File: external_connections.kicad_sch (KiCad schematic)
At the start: 14 parts, among them J1 FTDI_6P, J2 EXT_CLK_IN5, J3 PWR Test, J6 AVR-ISP-6, SW1 SW_Push

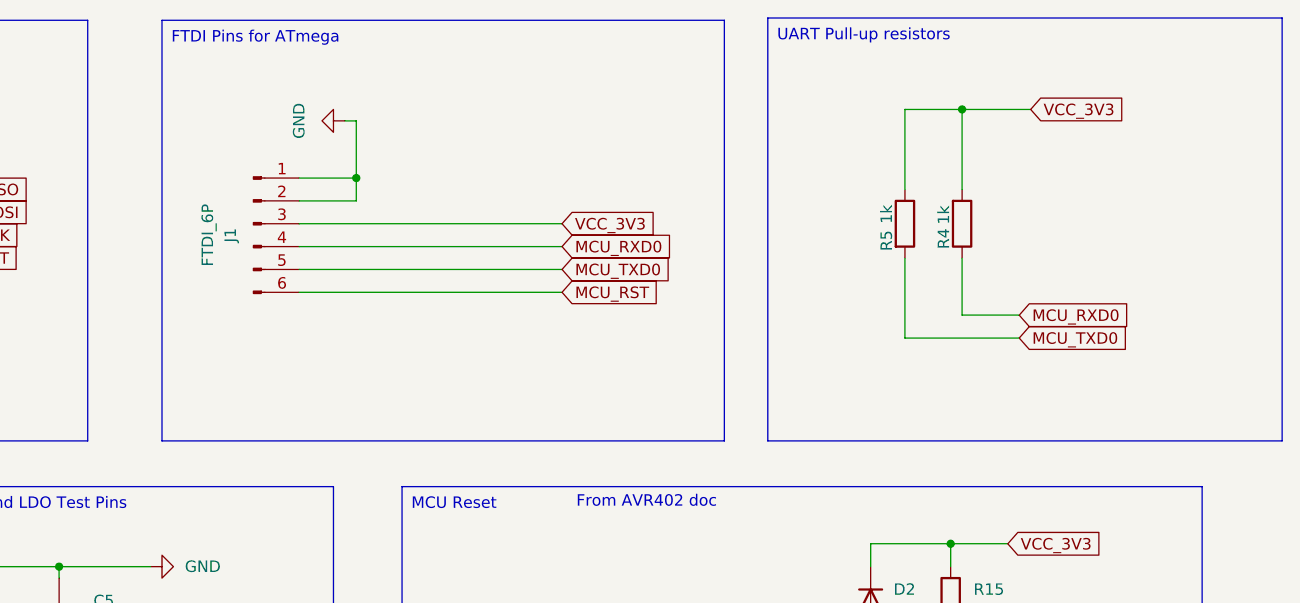
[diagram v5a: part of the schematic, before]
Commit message: inceased the size of some tp headers to 2.00mm
Signed-off-by: Mika Laitio <lamikr@gmail.com>
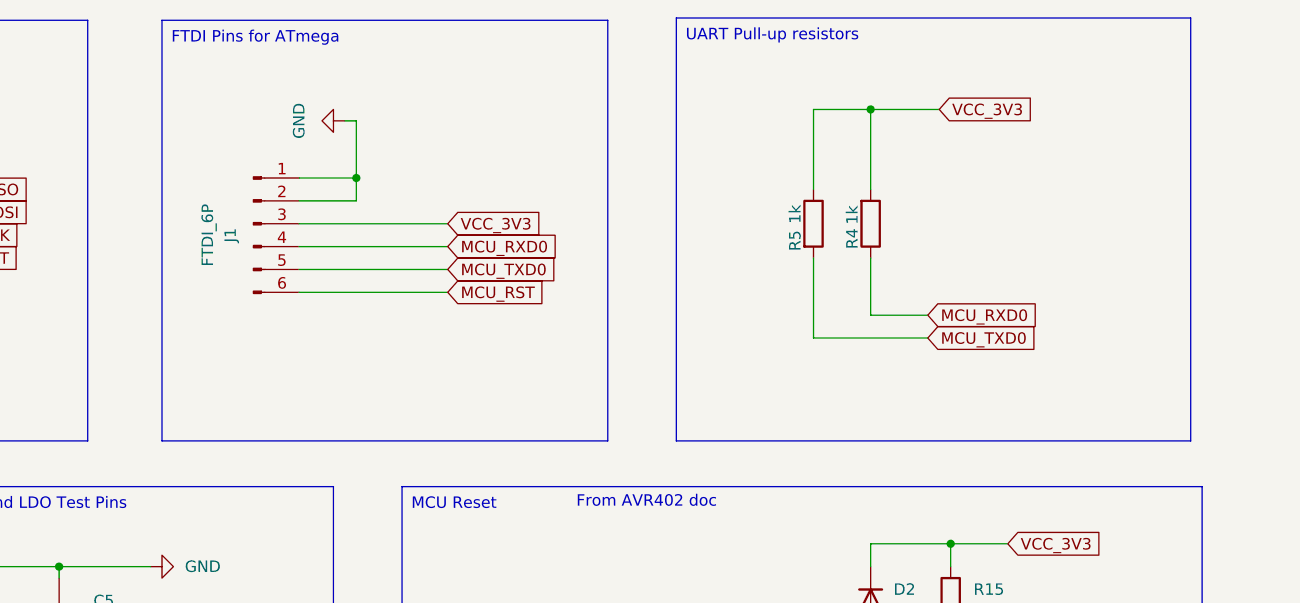
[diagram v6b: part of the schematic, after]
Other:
- moved on the sheet: R4, R5
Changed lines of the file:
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@@
 	)
 	(junction
-		(at 200.66 27.94)
+		(at 190.5 27.94)
 		(diameter 0)
 		(color 0 0 0 0)
@@
 	(wire
 		(pts
-			(xy 200.66 36.83) (xy 200.66 27.94)
-		)
-		(stroke
-			(width 0)
-			(type default)
-		)
-	)
-	(wire
-		(pts
-			(xy 200.66 27.94) (xy 208.28 27.94)
+			(xy 190.5 36.83) (xy 190.5 27.94)
+		)
+		(stroke
+			(width 0)
+			(type default)
+		)
+	)
+	(wire
+		(pts
+			(xy 190.5 27.94) (xy 198.12 27.94)
 		)
 		(stroke
@@
 	(wire
 		(pts
-			(xy 127 40.64) (xy 156.21 40.64)
+			(xy 127 40.64) (xy 143.51 40.64)
 		)
 		(stroke
@@
 	(wire
 		(pts
-			(xy 207.01 50.8) (xy 200.66 50.8)
+			(xy 196.85 50.8) (xy 190.5 50.8)
 		)
 		(stroke
@@
 	(wire
 		(pts
-			(xy 207.01 53.34) (xy 194.31 53.34)
+			(xy 196.85 53.34) (xy 184.15 53.34)
 		)
 		(stroke
@@
 	(wire
 		(pts
-			(xy 200.66 50.8) (xy 200.66 44.45)
-		)
-		(stroke
-			(width 0)
-			(type default)
-		)
-	)
-	(wire
-		(pts
-			(xy 127 48.26) (xy 156.21 48.26)
+			(xy 190.5 50.8) (xy 190.5 44.45)
+		)
+		(stroke
+			(width 0)
+			(type default)
+		)
+	)
+	(wire
+		(pts
+			(xy 127 48.26) (xy 143.51 48.26)
 		)
 		(stroke
@@
 	(wire
 		(pts
-			(xy 194.31 27.94) (xy 200.66 27.94)
+			(xy 184.15 27.94) (xy 190.5 27.94)
 		)
 		(stroke
@@
 	(wire
 		(pts
-			(xy 194.31 36.83) (xy 194.31 27.94)
+			(xy 184.15 36.83) (xy 184.15 27.94)
 		)
 		(stroke
@@
 	(wire
 		(pts
-			(xy 127 45.72) (xy 156.21 45.72)
+			(xy 127 45.72) (xy 143.51 45.72)
 		)
 		(stroke
@@
 	(wire
 		(pts
-			(xy 194.31 53.34) (xy 194.31 44.45)
+			(xy 184.15 53.34) (xy 184.15 44.45)
 		)
 		(stroke
@@
 	(wire
 		(pts
-			(xy 127 43.18) (xy 156.21 43.18)
+			(xy 127 43.18) (xy 143.51 43.18)
 		)
 		(stroke
@@
 	(text_box "UART Pull-up resistors"
 		(exclude_from_sim no)
-		(at 179.07 17.78 0)
+		(at 168.91 17.78 0)
 		(size 57.15 46.99)
 		(stroke
@@
 		(exclude_from_sim no)
 		(at 111.76 18.034 0)
-		(size 62.484 46.736)
+		(size 49.53 46.736)
 		(stroke
 			(width 0)
@@
 	(global_label "VCC_3V3"
 		(shape input)
-		(at 208.28 27.94 0)
+		(at 198.12 27.94 0)
 		(fields_autoplaced yes)
 		(effects
@@
 		)
 		(property "Intersheetrefs" "${INTERSHEET_REFS}"
-			(at 219.369 27.94 0)
+			(at 209.209 27.94 0)
 			(effects
 				(font
@@
 	(global_label "MCU_RXD0"
 		(shape input)
-		(at 207.01 50.8 0)
+		(at 196.85 50.8 0)
 		(fields_autoplaced yes)
 		(effects
@@
 		)
 		(property "Intersheetrefs" "${INTERSHEET_REFS}"
-			(at 219.9737 50.8 0)
+			(at 209.8137 50.8 0)
 			(effects
 				(font
@@
 	(global_label "MCU_RXD0"
 		(shape input)
-		(at 156.21 43.18 0)
+		(at 143.51 43.18 0)
 		(fields_autoplaced yes)
 		(effects
@@
 		)
 		(property "Intersheetrefs" "${INTERSHEET_REFS}"
-			(at 169.1737 43.18 0)
+			(at 156.4737 43.18 0)
 			(effects
 				(font
@@
 	(global_label "MCU_TXD0"
 		(shape input)
-		(at 207.01 53.34 0)
+		(at 196.85 53.34 0)
 		(fields_autoplaced yes)
 		(effects
@@
 		)
 		(property "Intersheetrefs" "${INTERSHEET_REFS}"
-			(at 219.6713 53.34 0)
+			(at 209.5113 53.34 0)
 			(effects
 				(font
@@
 	(global_label "MCU_TXD0"
 		(shape input)
-		(at 156.21 45.72 0)
+		(at 143.51 45.72 0)
 		(fields_autoplaced yes)
 		(effects
@@
 		)
 		(property "Intersheetrefs" "${INTERSHEET_REFS}"
-			(at 168.8713 45.72 0)
+			(at 156.1713 45.72 0)
 			(effects
 				(font
@@
 	(global_label "VCC_3V3"
 		(shape input)
-		(at 156.21 40.64 0)
+		(at 143.51 40.64 0)
 		(fields_autoplaced yes)
 		(effects
@@
 		)
 		(property "Intersheetrefs" "${INTERSHEET_REFS}"
-			(at 167.299 40.64 0)
+			(at 154.599 40.64 0)
 			(effects
 				(font
@@
 	(global_label "MCU_RST"
 		(shape input)
-		(at 156.21 48.26 0)
+		(at 143.51 48.26 0)
 		(fields_autoplaced yes)
 		(effects
@@
 		)
 		(property "Intersheetrefs" "${INTERSHEET_REFS}"
-			(at 167.6618 48.26 0)
+			(at 154.9618 48.26 0)
 			(effects
 				(font
@@
 	(symbol
 		(lib_id "Device:R")
-		(at 194.31 40.64 0)
+		(at 184.15 40.64 0)
 		(unit 1)
 		(exclude_from_sim no)
@@
 		(dnp no)
 		(property "Reference" "R5"
-			(at 192.278 43.688 90)
+			(at 182.118 43.688 90)
 			(effects
 				(font
@@
 		)
 		(property "Value" "1k"
-			(at 192.278 40.64 90)
+			(at 182.118 40.64 90)
 			(effects
 				(font
@@
 		)
 		(property "Footprint" "Resistor_SMD:R_0402_1005Metric"
-			(at 192.532 40.64 90)
+			(at 182.372 40.64 90)
 			(effects
 				(font
@@
 		)
 		(property "Datasheet" "~"
-			(at 194.31 40.64 0)
+			(at 184.15 40.64 0)
 			(effects
 				(font
@@
 		)
 		(property "Description" "Resistor"
-			(at 194.31 40.64 0)
+			(at 184.15 40.64 0)
 			(effects
 				(font
@@
 		)
 		(property "Notes" ""
-			(at 194.31 40.64 0)
+			(at 184.15 40.64 0)
 			(effects
 				(font
@@
 		)
 		(property "Price" "0.1"
-			(at 194.31 40.64 0)
+			(at 184.15 40.64 0)
 			(effects
 				(font
@@
 		)
 		(property "MFR" "Yageo"
-			(at 194.31 40.64 0)
+			(at 184.15 40.64 0)
 			(effects
 				(font
@@
 		)
 		(property "MPN" "RC0402FR-070RL"
-			(at 194.31 40.64 0)
+			(at 184.15 40.64 0)
 			(effects
 				(font
@@
 		)
 		(property "SKU_DIGIKEY" "311-0.0LRCT-ND"
-			(at 194.31 40.64 0)
+			(at 184.15 40.64 0)
 			(effects
 				(font
@@
 		)
 		(property "QtyOrdered" "100"
-			(at 194.31 40.64 0)
+			(at 184.15 40.64 0)
 			(effects
 				(font
@@
 	(symbol
 		(lib_id "Device:R")
-		(at 200.66 40.64 0)
+		(at 190.5 40.64 0)
 		(mirror x)
 		(unit 1)
@@
 		(dnp no)
 		(property "Reference" "R4"
-			(at 198.628 41.148 90)
+			(at 188.468 41.148 90)
 			(effects
 				(font
@@
 		)
 		(property "Value" "1k"
-			(at 198.628 38.608 90)
+			(at 188.468 38.608 90)
 			(effects
 				(font
@@
 		)
 		(property "Footprint" "Resistor_SMD:R_0402_1005Metric"
-			(at 198.882 40.64 90)
+			(at 188.722 40.64 90)
 			(effects
 				(font
@@
 		)
 		(property "Datasheet" "~"
-			(at 200.66 40.64 0)
+			(at 190.5 40.64 0)
 			(effects
 				(font
@@
 		)
 		(property "Description" "Resistor"
-			(at 200.66 40.64 0)
+			(at 190.5 40.64 0)
 			(effects
 				(font
@@
 		)
 		(property "Notes" ""
-			(at 200.66 40.64 0)
+			(at 190.5 40.64 0)
 			(effects
 				(font
@@
 		)
 		(property "Price" "0.1"
-			(at 200.66 40.64 0)
+			(at 190.5 40.64 0)
 			(effects
 				(font
@@
 		)
 		(property "MFR" "Yageo"
-			(at 200.66 40.64 0)
+			(at 190.5 40.64 0)
 			(effects
 				(font
@@
 		)
 		(property "MPN" "RC0402FR-0710KL"
-			(at 200.66 40.64 0)
+			(at 190.5 40.64 0)
 			(effects
 				(font
@@
 		)
 		(property "SKU_DIGIKEY" "311-10.0KLRCT-ND"
-			(at 200.66 40.64 0)
+			(at 190.5 40.64 0)
 			(effects
 				(font
@@
 		)
 		(property "QtyOrdered" "100"
-			(at 200.66 40.64 0)
-			(effects
-				(font
+			(at 190.5 40.64 0)
+			(effects
+				(font

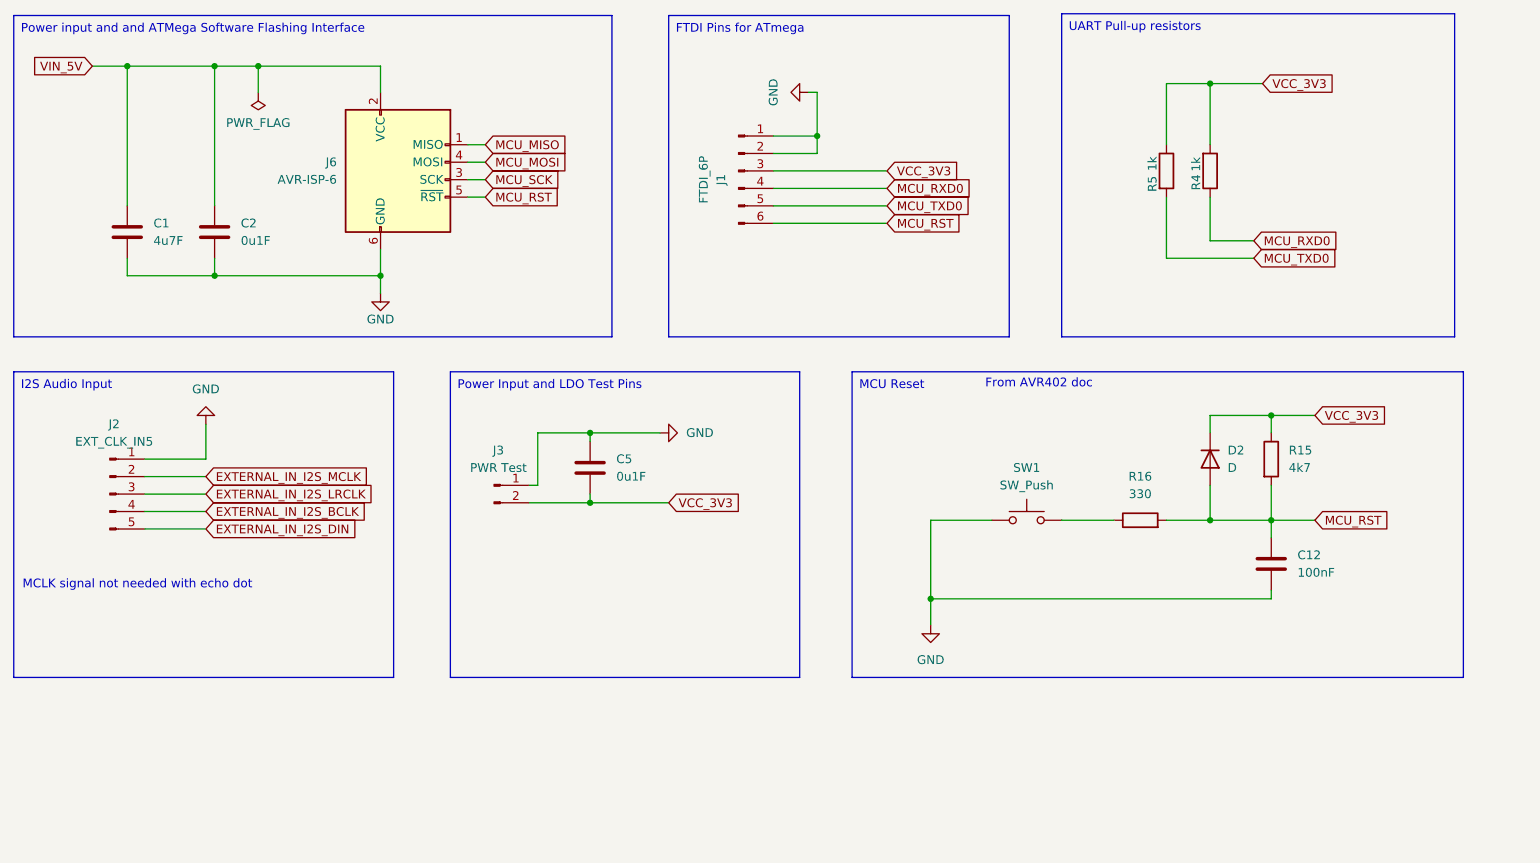
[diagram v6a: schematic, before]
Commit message: component footprint updates
- 0402 caps and resistors to 0603
- reset pin-header to reset button

Signed-off-by: Mika Laitio <lamikr@gmail.com>
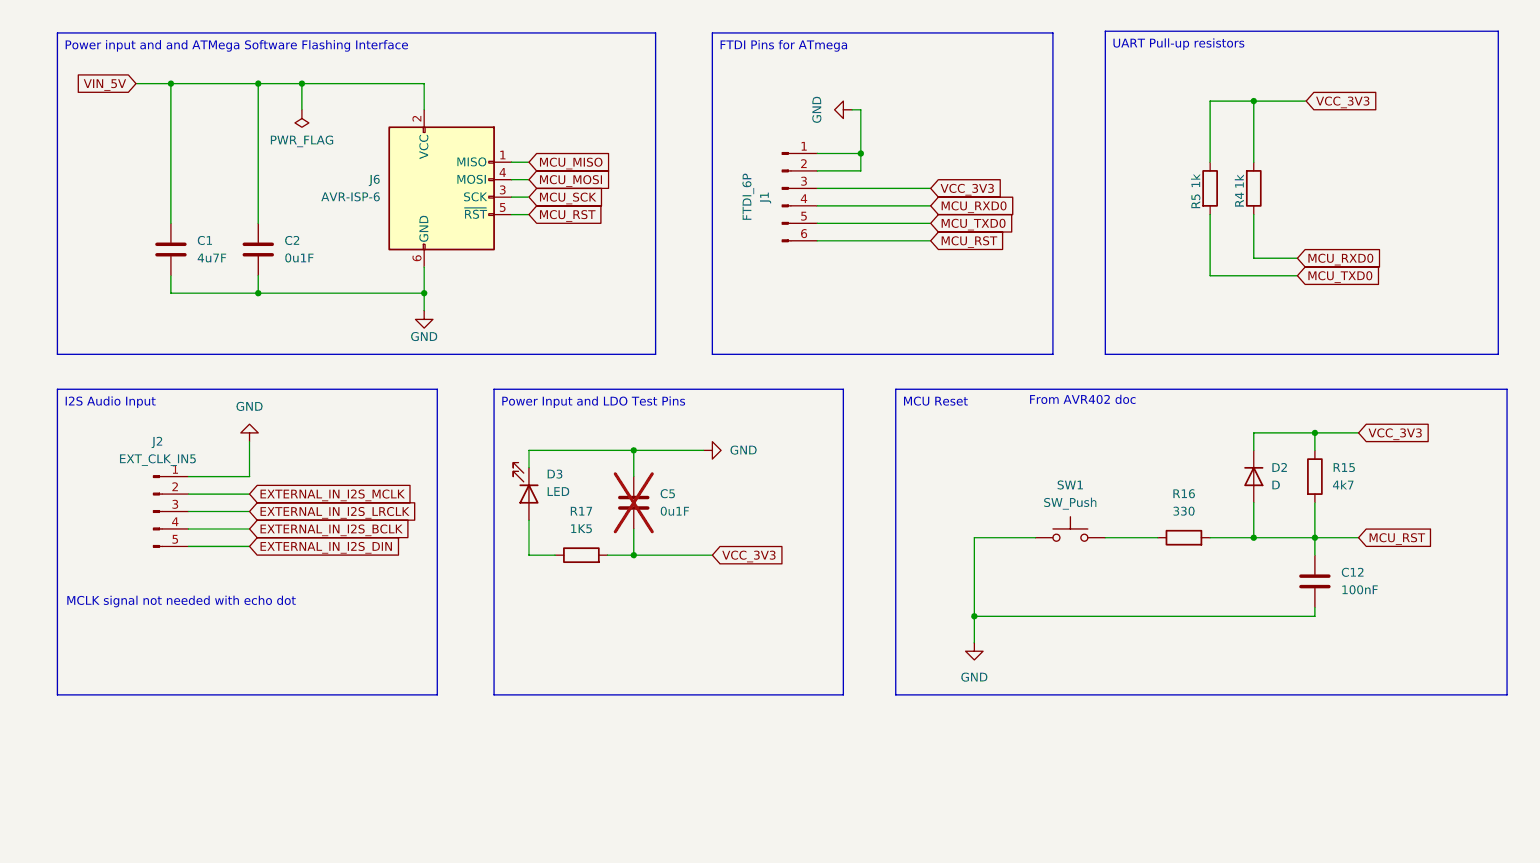
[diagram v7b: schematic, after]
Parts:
- removed J3: PWR Test, Connector_PinHeader_2.54mm:PinHeader_1x02_P2.54mm_Vertical, symbol Connector:Conn_01x02_Pin
- added D3: LED, LED_SMD:LED_0805_2012Metric, symbol Device:LED
- added R17: 1K5, Resistor_SMD:R_0603_1608Metric, symbol Device:R
- C1, C12, C2: footprint Capacitor_SMD:C_0402_1005Metric -> Capacitor_SMD:C_0603_1608Metric
- C5: footprint Capacitor_SMD:C_0402_1005Metric -> Capacitor_SMD:C_0603_1608Metric; now not fitted
- D2: footprint Diode_SMD:D_0402_1005Metric -> Diode_SMD:D_0603_1608Metric
- R15, R16, R4, R5: footprint Resistor_SMD:R_0402_1005Metric -> Resistor_SMD:R_0603_1608Metric
- SW1: footprint Connector_PinHeader_2.54mm:PinHeader_1x02_P2.54mm_Vertical -> Button_Switch_SMD:SW_SPST_B3U-1000P
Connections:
- net GND: now also D3.1 (K)
- net VCC_3V3: now also R17.2
- new net: D3.2 (A), R17.1
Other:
- moved on the sheet: C1, C12, C2, D2, J1, J2, J6, R15, R16, R4, R5, SW1

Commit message: rework the atmega168 reset signal schematics and routing
Signed-off-by: Mika Laitio <lamikr@gmail.com>
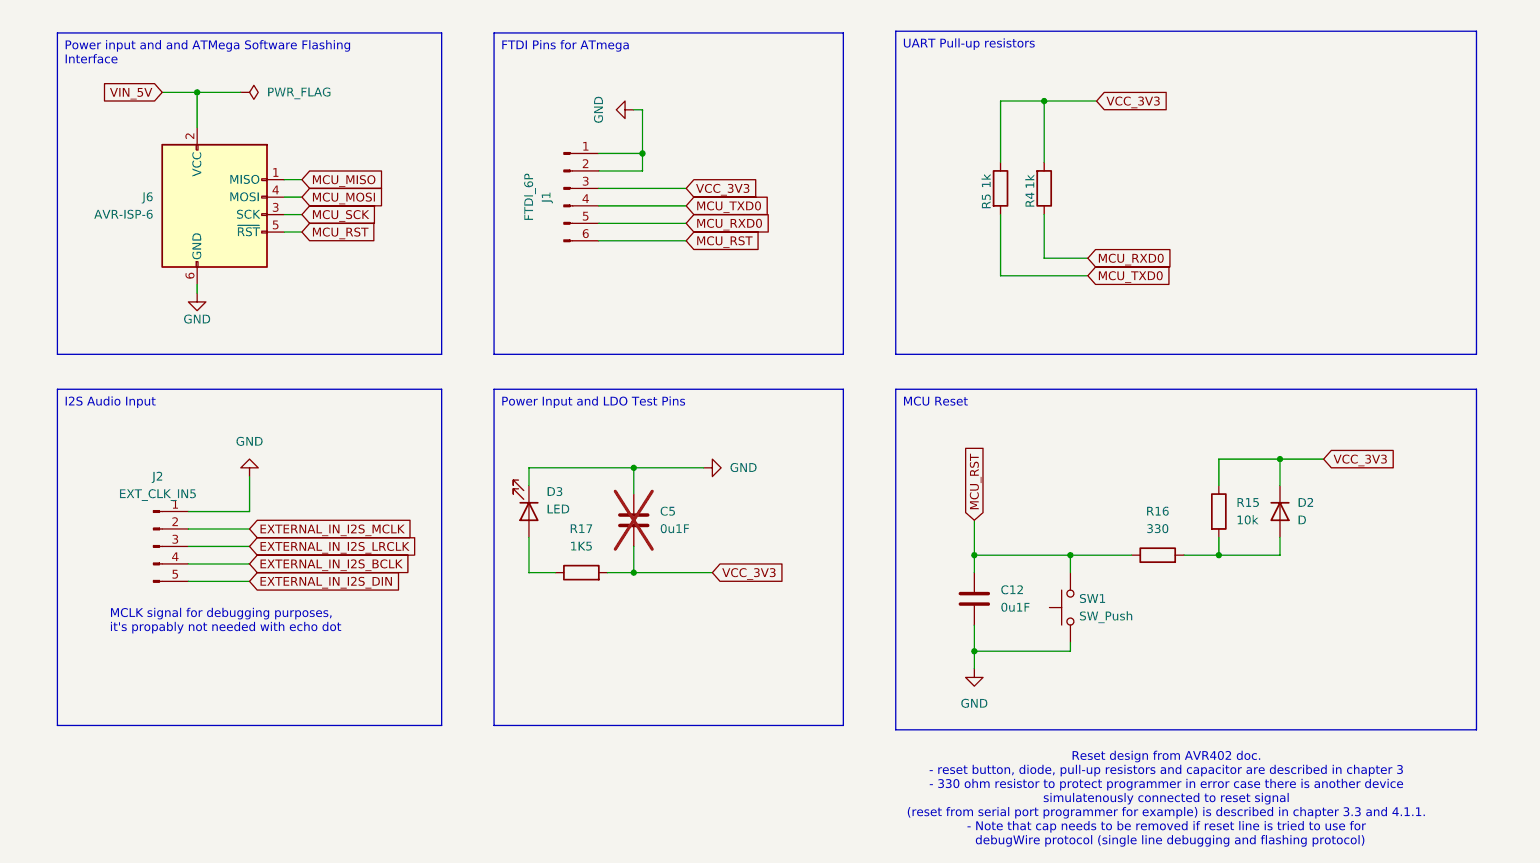
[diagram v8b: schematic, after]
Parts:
- removed C1: 4u7F, Capacitor_SMD:C_0603_1608Metric, symbol Device:C
- removed C2: 0u1F, Capacitor_SMD:C_0603_1608Metric, symbol Device:C
- C12: value 100nF -> 0u1F
- R15: value 4k7 -> 10k
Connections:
- net MCU_RST: now also R16.1, SW1.2; no longer D2.2 (A), R15.2, R16.2
- net MCU_RXD0: now also J1.5 (Pin_5); no longer J1.4 (Pin_4)
- net MCU_TXD0: now also J1.4 (Pin_4); no longer J1.5 (Pin_5)
- new net: D2.2 (A), R15.2, R16.2
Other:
- note added: "MCLK signal for debugging purposes, it's propably not needed with echo dot"
- note added: "Reset design from AVR402 doc. - reset button, diode, pull-up resistors and capacitor are described in chapter 3 - 330 ohm resistor to protect programmer in error case there is another device simulatenously connected to reset signal (reset from serial port programmer for example) is described in chapter 3.3 and 4.1.1. - Note that cap needs to be removed if reset line is tried to use for debugWire 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"
- note removed: "From AVR402 doc"
- note removed: "MCLK signal not needed with echo dot"
- moved on the sheet: C12, C5, D2, D3, J1, J2, J6, R15, R16, R17, R4, R5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
